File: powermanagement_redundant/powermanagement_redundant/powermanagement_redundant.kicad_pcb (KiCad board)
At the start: 2 copper layers, 115.2 x 22.5 mm, 25 parts, among them J1 Screw_Terminal_01x01, J2 Screw_Terminal_01x01, J3 Screw_Terminal_01x01, J4 Screw_Terminal_01x01, J5 Screw_Terminal_01x01, J6 Screw_Terminal_01x01, J7 Screw_Terminal_01x01, J8 Screw_Terminal_01x01, J9 691323300002, Q1 BUK9M11-40EX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

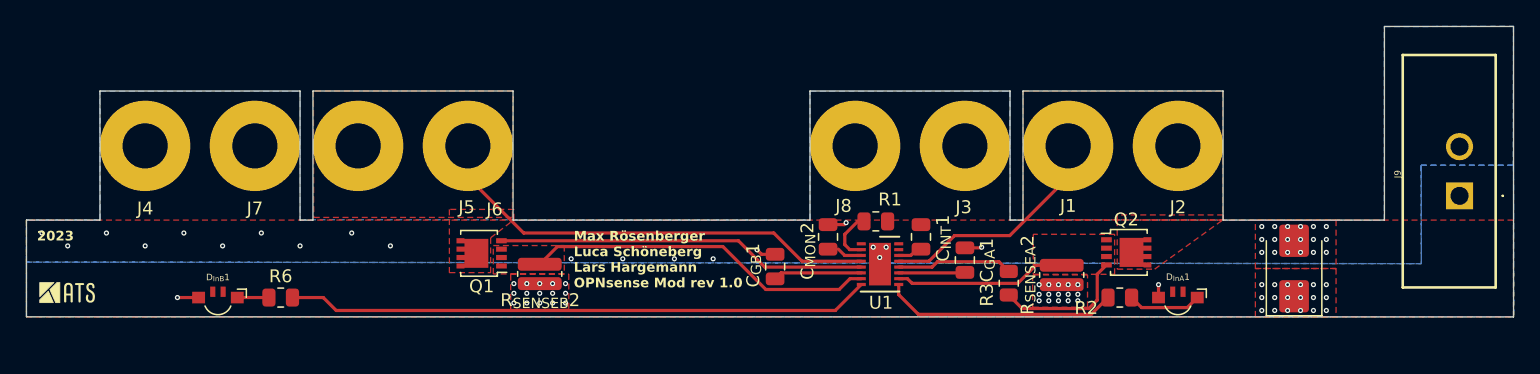
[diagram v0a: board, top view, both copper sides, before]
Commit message: N-Channel MOSFET falsche Orientierung
Die Orientierung des N-MOSFET ist geändert. Vor der Fertigung muss noch auf der PCB die Versions Nummer geändert werden.
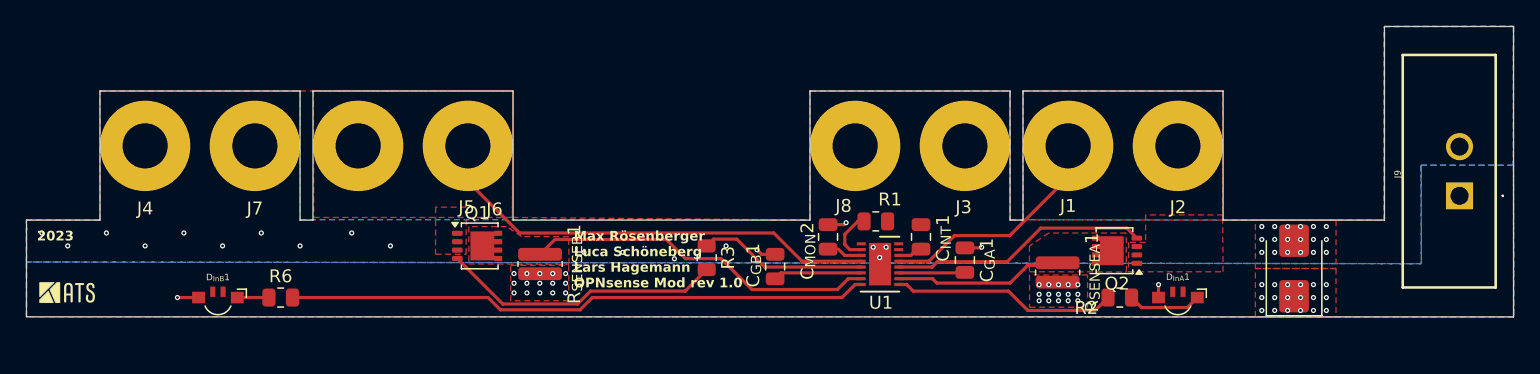
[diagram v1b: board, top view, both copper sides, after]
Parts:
- removed R_{SENSEA}2, R_{SENSEB}2: 2m 1% 2W, Resistor_SMD:R_0612_1632Metric
- added R_{SENSEA}1: 2m 1% 2W, Resistor_SMD:R_0612_1632Metric, F.Cu at (105.7, 34.1)
- added R_{SENSEB}1: 2m 1% 2W, Resistor_SMD:R_0612_1632Metric, F.Cu at (65.6, 33.4)
- moved R3 23.5 mm to (78.5, 32.9)
- moved Q2 0.73 mm to (110.3, 32.4), turned to 180 degrees
- moved Q1 0.67 mm to (60.7, 32.0), turned to 0 degrees
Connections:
- Q1 pad 1: SENB -> INB
- Q1 pad 2: SENB -> INB
- Q1 pad 3: SENB -> INB
- Q1 pad 4: GTB -> Net-(Q1-G)
- Q1 pad 5: INB -> SENB
- Q2 pad 1: SENA -> INA
- Q2 pad 2: SENA -> INA
- Q2 pad 3: SENA -> INA
- Q2 pad 4: Net-(Q2-G) -> GTA
- Q2 pad 5: INA -> SENA
- R3 pad 1: GTA -> GTB
- R3 pad 2: Net-(Q2-G) -> Net-(Q1-G)
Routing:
- net Net-(Q1-G): track 0.00 -> 21.9 mm
- net GTB: track 28.7 -> 13.1 mm
- net GTA: track 9.01 -> 20.0 mm
- net Net-(Q2-G): track 10.6 -> 0.00 mm
- net PGA: track 18.2 -> 17.5 mm
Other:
- board text added: "Max Rösenberger Luca Schöneberg Lars Hagemann OPNsense Mod rev 1.0"
- board text removed: "Max Rösenberger Luca Schöneberg Lars Hargemann OPNsense Mod rev 1.0"

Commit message: fix some issues for Aisler Order
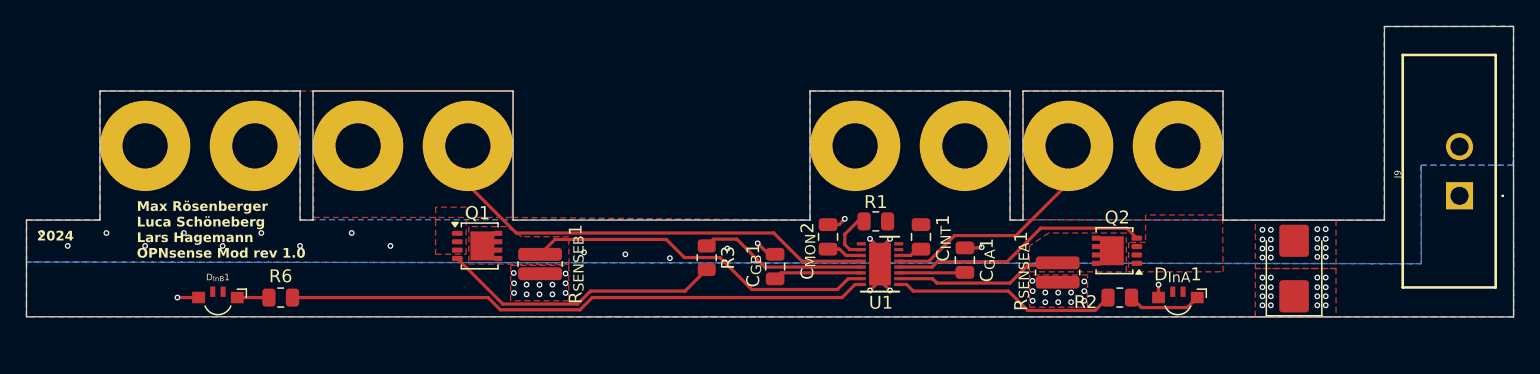
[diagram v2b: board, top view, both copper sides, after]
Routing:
- net GND: track 7.92 -> 11.6 mm, vias 38 -> 37
- net COMP: track 1.98 -> 2.78 mm
- net LOAD: vias 50 -> 42
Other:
- board text added: "2024"
- board text removed: "2023"
